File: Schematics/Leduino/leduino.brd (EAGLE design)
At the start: 88.6 x 63.5 mm, 31 parts, among them J1 POWER_JACKCOMBO

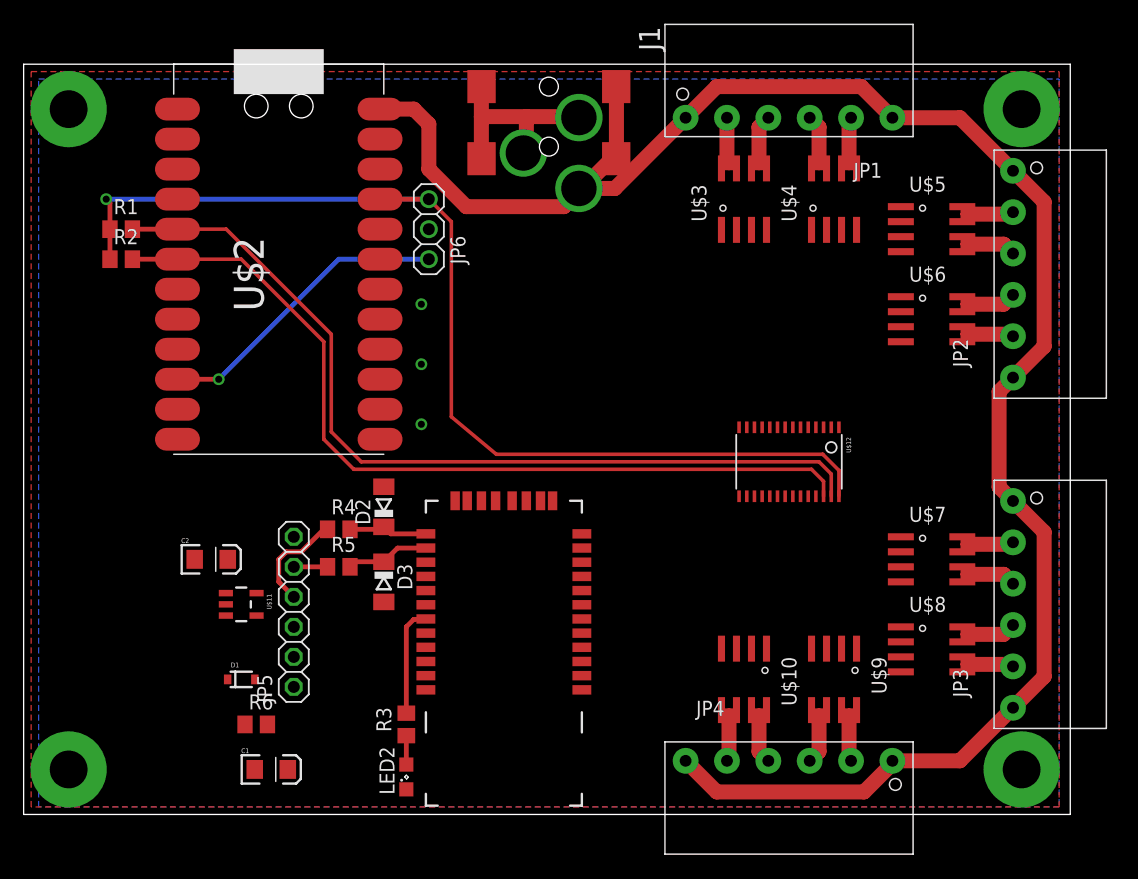
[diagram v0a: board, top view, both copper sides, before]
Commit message: Making progress, attempting to hack the autorouter
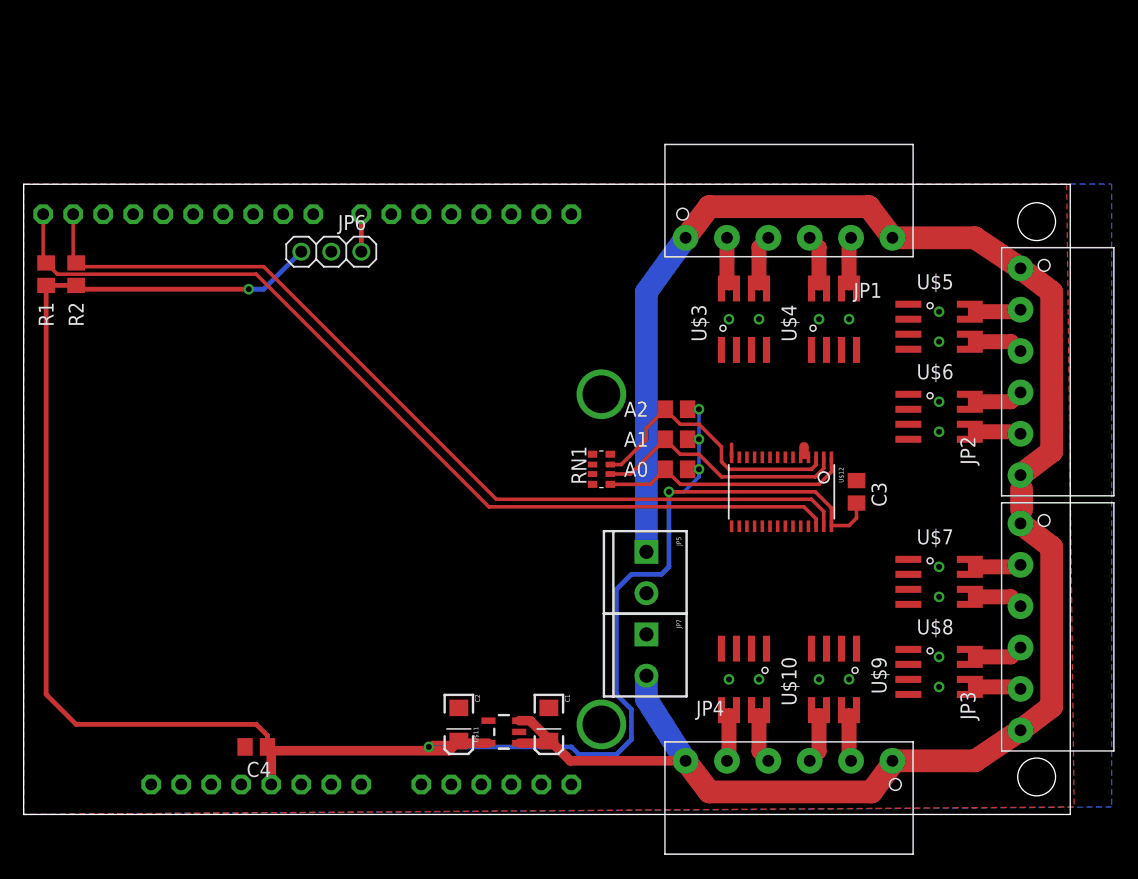
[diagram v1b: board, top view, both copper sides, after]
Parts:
- removed D1: (no value), SparkFun:SOD-323
- removed D2: 3.3V, diode:SOD80C
- removed D3: 3.3v, diode:SOD80C
- removed J1: POWER_JACKCOMBO, SparkFun-Connectors:POWER_JACK_COMBO
- removed LED2: RED, led:SML0805
- removed R3: 1K, rcl:R0805
- removed R4, R5: 10K, rcl:R0805
- removed R6: 0Ohm DNP, rcl:R0805
- removed U$2: PRO_MICRO, Leduino:ARDUINO_PRO_MICRO_SMD
- added A0, A1, A2: 0 Ohm DNP, rcl:R0805
- added C3, C4: .1uF, rcl:C0805
- added JP7: M023.5MM, SparkFun-Connectors:SCREWTERMINAL-3.5MM-2
- added RN1: (no value), resistor-dil:EXB38V
- JP5: value FTDI_CABLE -> M023.5MM; device Leduino:1X06 -> SparkFun-Connectors:SCREWTERMINAL-3.5MM-2
- U$1: value BLUETOOTH-RN41" -> SHIELD; device Leduino:RN41 -> Leduino:ARDUINOR3
- U$11: value MIC5219-3.3YM5 -> MIC5219-5.0YM5
- moved U$1 60.3 mm to (-17.1, 0.00), turned to 0 degrees
- moved JP5 30.3 mm to (52.7, 22.2), turned to 270 degrees
- moved C2 25.2 mm to (36.8, 7.62), turned to 270 degrees
- moved U$11 24.7 mm to (40.6, 6.99), turned to 90 degrees
- moved C1 23.8 mm to (44.5, 7.62), turned to 270 degrees
- moved JP1 10.2 mm to (64.8, 50.8)
- moved U$3 10.2 mm to (61.0, 41.9)
- moved U$4 10.2 mm to (68.6, 41.9)
- moved JP6 8.47 mm to (26.0, 47.6), turned to 0 degrees
- moved U$5 8.28 mm to (77.5, 41.3)
- moved JP2 8.28 mm to (86.4, 37.5)
- moved U$6 8.28 mm to (77.5, 33.7)
- moved R2 6.48 mm to (1.91, 45.7), turned to 90 degrees
- moved R1 5.39 mm to (4.45, 45.7), turned to 90 degrees
- moved U$12 2.62 mm to (64.1, 27.3)
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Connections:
- removed net CTS: JP5.2
- removed net FTDI_VCC: D1.2, JP5.3
- removed net N$13: R3.2, U$1.19
- removed net N$14: D2.C, R4.2, U$1.13
- removed net N$38: LED2.A, R3.1
- removed net RTS: JP5.6
- removed net RX: JP5.5, R5.1, U$2.2
- removed net TX: JP5.4, R4.1, U$2.1
- removed net V33: C2.A, R6.2, U$1.11, U$11.5
- new net N$16: A1.1, RN1.6, U$12.2
- new net N$21: A2.1, RN1.7, U$12.3
- net GND: now also C3.2, C4.2, JP5.2, JP7.1, RN1.1, RN1.2, RN1.3, RN1.4, U$1.GND, U$1.GND1, U$1.GND2; no longer D2.A, D3.A, J1.GND, J1.GND@1, JP5.1, LED2.C, U$1.1, U$1.12, U$1.28, U$1.29, U$12.1, U$12.2, U$12.3, U$2.19, U$2.20, U$2.23, U$2.3, U$2.4, U$2.8, U$2.9
- net IR_INT: now also U$1.D7; no longer U$2.10
- net N$15: now also A0.1, RN1.5, U$12.1; no longer D3.C, R5.2, U$1.14
- net SCL: now also U$1.SCL; no longer U$2.6
- net SDA: now also U$1.SDA; no longer U$2.5
- net VCC: now also A0.2, A1.2, A2.2, C2.A, C3.1, C4.1, U$1.5V, U$11.5; no longer R6.1, U$2.21
- net VIN: now also JP5.1, JP7.2; no longer D1.1, J1.POWER, U$2.24
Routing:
- net VCC: track 92.6 -> 180.6 mm, vias 1 -> 6
- net N$21: track 0.00 -> 23.6 mm
- net IR_INT: track 25.5 -> 3.17 mm, vias 1 -> 0
- net N$16: track 0.00 -> 21.8 mm
- net N$15: track 7.08 -> 21.4 mm
- net VIN: track 149.2 -> 162.0 mm
- net N$13: track 9.24 -> 0.00 mm
- net TX: track 8.88 -> 0.00 mm
- net N$14: track 6.75 -> 0.00 mm
- net SCL: track 73.1 -> 79.0 mm
- net SDA: track 74.4 -> 77.6 mm
- net GND: track 0.00 -> 2.87 mm, vias 7 -> 18
- net RX: track 2.86 -> 0.00 mm
- net N$38: track 2.45 -> 0.00 mm
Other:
- board size 88.6 x 63.5 mm -> 88.6 x 53.3 mm

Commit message: Finished Layout, cleared DRC
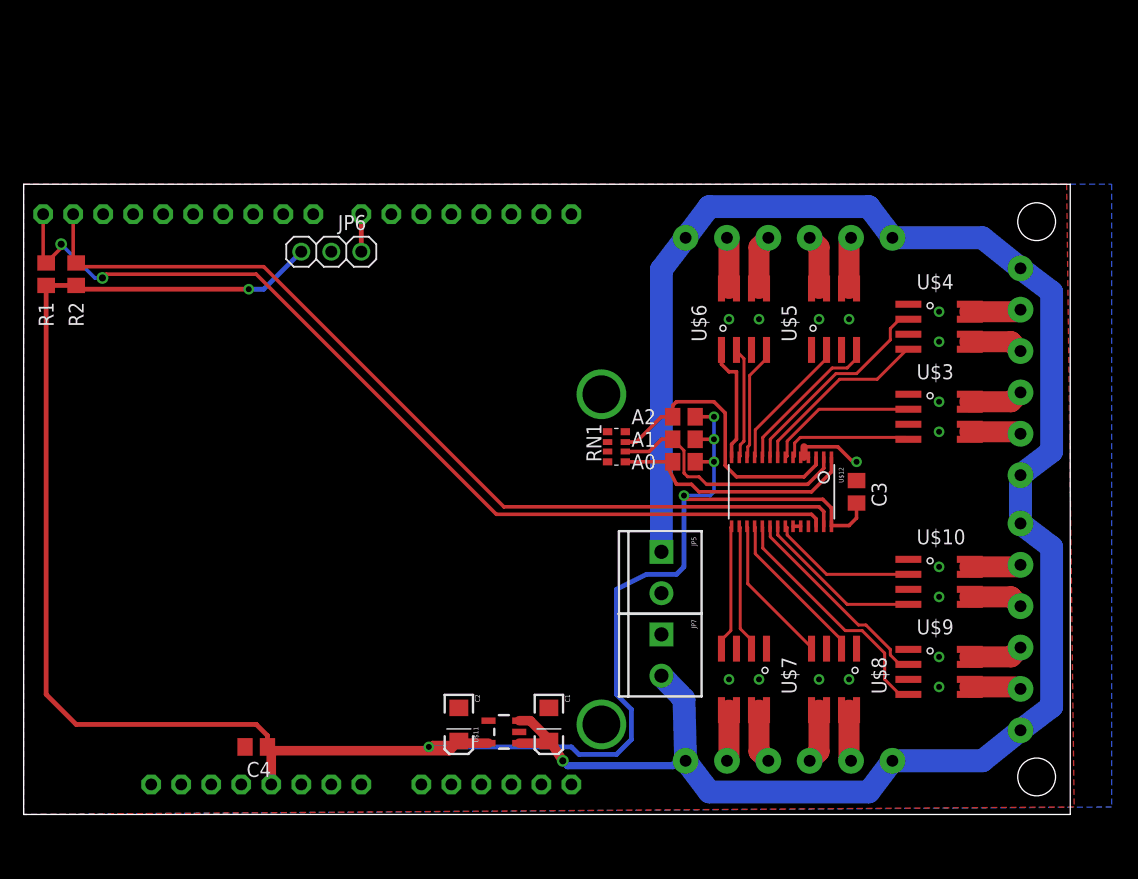
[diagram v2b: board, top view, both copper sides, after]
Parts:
- U$10, U$3, U$4, U$5, U$6, U$7, U$8, U$9: value (none) -> DMN6040SSD
- moved JP3 25.4 mm to (64.8, 2.54), flipped to the bottom, turned to 180 degrees
- moved JP4 25.4 mm to (86.4, 15.9), flipped to the bottom, turned to 90 degrees
- moved JP1 25.4 mm to (86.4, 37.5), flipped to the bottom, turned to 90 degrees
- moved JP2 25.4 mm to (64.8, 50.8), flipped to the bottom, turned to 0 degrees
- moved U$10 18.5 mm to (77.5, 19.7), turned to 270 degrees
- moved U$7 18.5 mm to (61.0, 11.4), turned to 180 degrees
- moved U$3 18.5 mm to (77.5, 33.7), turned to 270 degrees
- moved U$6 18.5 mm to (61.0, 41.9), turned to 0 degrees
- moved U$4 8.91 mm to (77.5, 41.3), turned to 270 degrees
- moved U$5 8.91 mm to (68.6, 41.9), turned to 0 degrees
- moved U$8 8.91 mm to (68.6, 11.4), turned to 180 degrees
- moved U$9 8.91 mm to (77.5, 12.1), turned to 270 degrees
- moved RN1 2.29 mm to (50.2, 31.1)
- moved JP5 1.27 mm to (54.0, 22.2)
- moved JP7 1.27 mm to (54.0, 15.2)
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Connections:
- net N$1: now also U$3.5, U$3.6; no longer U$3.7, U$3.8
- net N$10: now also U$5.7, U$5.8; no longer U$5.5, U$5.6
- net N$11: now also U$6.7, U$6.8; no longer U$6.5, U$6.6
- net N$12: now also U$6.5, U$6.6; no longer U$6.7, U$6.8
- net N$17: now also U$7.5, U$7.6; no longer U$7.7, U$7.8
- net N$18: now also U$7.7, U$7.8; no longer U$7.5, U$7.6
- net N$19: now also U$8.7, U$8.8; no longer U$8.5, U$8.6
- net N$2: now also U$3.7, U$3.8; no longer U$3.5, U$3.6
- net N$20: now also U$8.5, U$8.6; no longer U$8.7, U$8.8
- net N$3: now also U$4.7, U$4.8; no longer U$4.5, U$4.6
- net N$4: now also U$4.5, U$4.6; no longer U$4.7, U$4.8
- net N$5: now also U$9.5, U$9.6; no longer U$9.7, U$9.8
- net N$6: now also U$9.7, U$9.8; no longer U$9.5, U$9.6
- net N$7: now also U$10.7, U$10.8; no longer U$10.5, U$10.6
- net N$8: now also U$10.5, U$10.6; no longer U$10.7, U$10.8
- net N$9: now also U$5.5, U$5.6; no longer U$5.7, U$5.8
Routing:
- net PWM12: track 0.00 -> 20.6 mm
- net PWM3: track 0.00 -> 18.0 mm
- net PWM13: track 0.00 -> 17.3 mm
- net PWM2: track 0.00 -> 15.6 mm
- net GND: track 2.87 -> 17.9 mm, vias 18 -> 19
- net PWM14: track 0.00 -> 14.2 mm
- net PWM11: track 0.00 -> 13.4 mm
- net PWM4: track 0.00 -> 13.1 mm
- net PWM1: track 0.00 -> 12.8 mm
- net PWM10: track 0.00 -> 12.6 mm
- net PWM15: track 0.00 -> 12.5 mm
- net PWM5: track 0.00 -> 11.6 mm
- net PWM0: track 0.00 -> 11.2 mm
- net PWM9: track 0.00 -> 10.8 mm
- net PWM8: track 0.00 -> 10.7 mm
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
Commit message: Cleaned up silkscreen, passed freedDFM
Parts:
- JP1, JP2: value (none) -> M023.5MM; device Leduino:1X06-3.5M-RA -> SparkFun-Connectors:SCREWTERMINAL-3.5MM-2
- JP3: device Leduino:1X06-3.5M-RA -> adafruit:1X03
- JP5, JP7: value M023.5MM -> (none); device SparkFun-Connectors:SCREWTERMINAL-3.5MM-2 -> Leduino:1X06-3.5M-RA
- JP6: device adafruit:1X03 -> Leduino:1X06-3.5M-RA
- moved JP3 59.4 mm to (26.0, 47.6), flipped to the top, turned to 0 degrees
- moved JP6 59.4 mm to (64.8, 2.54), flipped to the bottom, turned to 180 degrees
- moved JP1 39.3 mm to (54.0, 15.2), flipped to the top, turned to 270 degrees
- moved JP7 32.4 mm to (86.4, 15.9), flipped to the bottom, turned to 90 degrees
- moved JP2 30.5 mm to (54.0, 22.2), flipped to the top, turned to 270 degrees
- moved JP5 30.5 mm to (64.8, 50.8), flipped to the bottom, turned to 0 degrees
- moved JP4 21.6 mm to (86.4, 37.5)
- renumbered U$1 to S1, U$10 to U10, U$11 to U1, U$12 to U2, U$3 to U3, U$4 to U4, U$5 to U5, U$6 to U6, U$7 to U7, U$8 to U8, U$9 to U9
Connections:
- net GND: now also JP1.1, JP2.2, JP3.2; no longer JP5.2, JP6.2, JP7.1
- net IR_INT: now also JP3.3; no longer JP6.3
- net N$1: now also JP4.2; no longer JP1.2
- net N$10: now also JP5.3; no longer JP2.3
- net N$11: now also JP5.5; no longer JP2.5
- net N$12: now also JP5.4; no longer JP2.4
- net N$17: now also JP6.2; no longer JP3.2
- net N$18: now also JP6.3; no longer JP3.3
- net N$19: now also JP6.5; no longer JP3.5
- net N$2: now also JP4.3; no longer JP1.3
- net N$20: now also JP6.4; no longer JP3.4
- net N$3: now also JP4.5; no longer JP1.5
- net N$4: now also JP4.4; no longer JP1.4
- net N$5: now also JP7.2; no longer JP4.2
- net N$6: now also JP7.3; no longer JP4.3
- net N$7: now also JP7.5; no longer JP4.5
- net N$8: now also JP7.4; no longer JP4.4
- net N$9: now also JP5.2; no longer JP2.2
- net VCC: now also JP3.1; no longer JP6.1
- net VIN: now also JP1.2, JP5.6, JP6.1, JP6.6, JP7.1, JP7.6; no longer JP1.1, JP1.6, JP2.6, JP3.1, JP3.6, JP7.2
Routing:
- net GND: vias 19 -> 23
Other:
- board text added: "0"
- board text added: "1"
- board text added: "10"
- board text added: "11"
- board text added: "12"
- board text added: "13"
- board text added: "14"
- board text added: "15"
- board text added: "2"
- board text added: "3"
- board text added: "4"
- board text added: "5"
- board text added: "6"
- board text added: "7"
- board text added: "8"
- board text added: "9"
- board text added: "LEDuino PWM Sheild Version 0.1.0 (C) 2014, Nathaniel Chapman nathanielchapman.com"

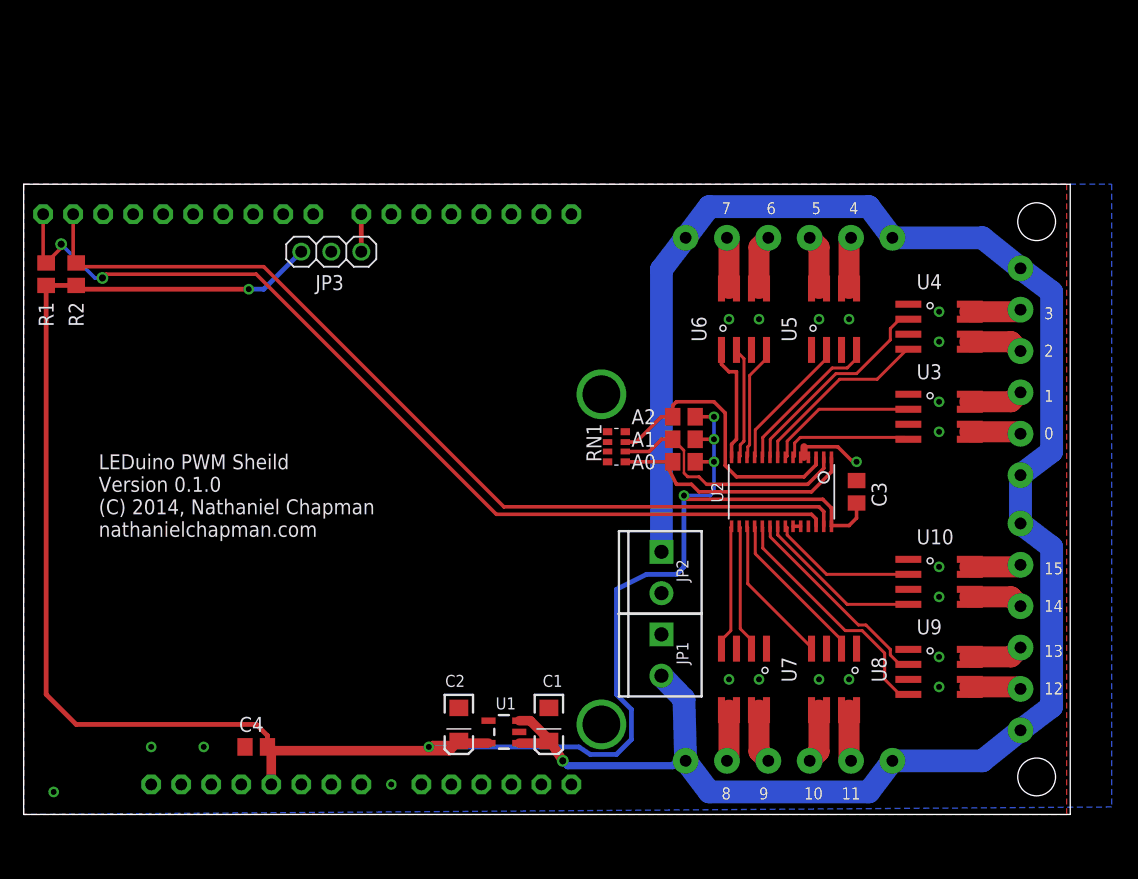
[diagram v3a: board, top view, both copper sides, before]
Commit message: Designed and Laid out Board Rev 2.0 ready for review
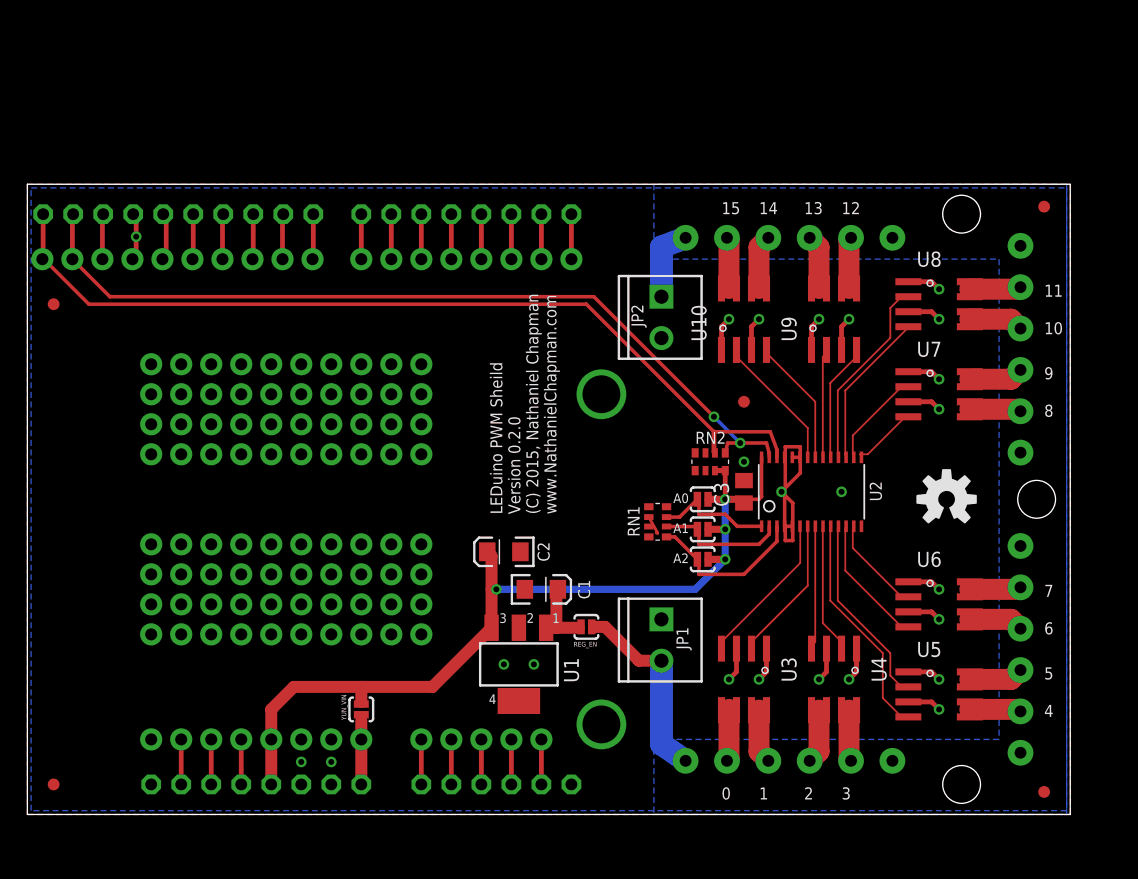
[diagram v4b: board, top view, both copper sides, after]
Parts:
- removed C4: .1uF, rcl:C0805
- removed R1, R2: 10K, rcl:R0805
- added JP10: (no value), SparkFun-Connectors:1X05_NO_SILK
- added JP8, JP9: (no value), SparkFun-Connectors:1X08_NO_SILK
- added NC1, NC2, NC3, NC4: PROTOBOARD5X4, Leduino:5X4_PROTO
- added REG_EN, YUN_VIN: (no value), Leduino:SJ_2S-NO
- added RN2: 10K, resistor-dil:EXB38V
- added U$1, U$2, U$4, U$5: (no value), Pro_Micro:FIDUCIAL-1X2
- added U$3: (no value), Pro_Micro:OSHW-LOGO-M
- A0, A1, A2: value 0 Ohm DNP -> (none); device rcl:R0805 -> Leduino:SJ_2S-NO
- JP3: device adafruit:1X03 -> SparkFun-Connectors:1X10_NO_SILK
- RN1: value (none) -> 10K
- U1: value MIC5219-5.0YM5 -> MIC39100-5.0WS; device SparkFun:SOT23-5 -> Leduino:SOT223
- moved JP5 42.7 mm to (86.4, 14.0), turned to 90 degrees
- moved JP6 42.7 mm to (86.4, 39.4), turned to 90 degrees
- moved JP4 41.1 mm to (64.8, 2.54), turned to 180 degrees
- moved JP7 41.1 mm to (64.8, 50.8), turned to 0 degrees
- moved U8 33.0 mm to (77.5, 43.2), turned to 270 degrees
- moved U5 33.0 mm to (77.5, 10.2), turned to 270 degrees
- moved U4 31.1 mm to (68.6, 11.4), turned to 180 degrees
- moved U9 31.1 mm to (68.6, 41.9), turned to 0 degrees
- moved U7 29.2 mm to (77.5, 35.6), turned to 270 degrees
- moved U6 29.2 mm to (77.5, 17.8), turned to 270 degrees
- moved U3 27.7 mm to (61.0, 11.4), turned to 180 degrees
- moved U10 27.7 mm to (61.0, 41.9), turned to 0 degrees
- moved JP3 24.5 mm to (1.59, 47.0)
- moved JP2 21.6 mm to (54.0, 43.8)
- moved C2 15.1 mm to (40.6, 22.2), turned to 180 degrees
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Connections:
- removed net IR_INT: JP3.3, S1.D7
- new net 3.3V: JP9.4, S1.3V
- new net A0: JP10.5, S1.A0
- new net A1: JP10.4, S1.A1
- new net A2: JP10.3, S1.A2
- new net A3: JP10.2, S1.A3
- new net A4: JP10.1, S1.A4
- new net A5: S1.A5
- new net AREF: JP3.3, S1.AREF
- new net D0: JP8.8, S1.D0
- new net D1: JP8.7, S1.D1
- new net D10: JP3.8, S1.D10
- new net D11: JP3.7, S1.D11
- new net D12: JP3.6, S1.D12
- new net D13: JP3.5, S1.D13
- new net D2: JP8.6, S1.D2
- new net D3: JP8.5, S1.D3
- new net D4: JP8.4, S1.D4
- new net D5: JP8.3, S1.D5
- new net D6: JP8.2, S1.D6
- new net D7: JP8.1, S1.D7
- new net D8: JP3.10, S1.D8
- new net D9: JP3.9, S1.D9
- new net IOREF: JP9.2, S1.IOREF
- new net N$13: C1.A, REG_EN.2, U1.1
- new net NC: JP9.1
- new net RES: JP9.3, S1.RESET
- new net VIN_A: JP9.8, S1.VIN, YUN_VIN.1
- net GND: now also JP3.4, JP9.6, JP9.7, RN1.8, U1.4; no longer C4.2, JP3.2
- net N$15: now also RN1.7; no longer RN1.5
- net N$21: now also RN1.5; no longer RN1.7
- net SCL: now also JP3.1, RN2.2; no longer R2.2
- net SDA: now also JP3.2, RN2.1; no longer R1.2
- net VCC: now also JP9.5, RN2.7, RN2.8, U1.3, YUN_VIN.2; no longer C4.1, JP3.1, R1.1, R2.1, U1.5
- net VIN: now also REG_EN.1; no longer C1.A, U1.1, U1.3
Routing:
- net VIN: track 162.1 -> 23.0 mm, vias 1 -> 0
- net VCC: track 181.4 -> 77.3 mm, vias 6 -> 4
- net GND: track 17.9 -> 72.1 mm, vias 23 -> 26
- net N$15: track 21.5 -> 10.3 mm
- net N$21: track 24.4 -> 13.8 mm
- net PWM12: track 20.6 -> 10.0 mm
- net N$16: track 21.4 -> 11.0 mm
- net PWM13: track 17.3 -> 9.22 mm
- net PWM3: track 18.0 -> 11.0 mm
- net N$13: track 0.00 -> 6.33 mm
- net PWM4: track 13.1 -> 19.2 mm
- net VIN_A: track 0.00 -> 5.90 mm
- net SDA: track 77.6 -> 72.2 mm, vias 0 -> 2
- net SCL: track 80.8 -> 75.5 mm, vias 2 -> 0
- net PWM2: track 15.6 -> 10.5 mm
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- added copper zone on layer 16, net VIN
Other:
- board size 88.6 x 53.3 mm -> 88.3 x 53.3 mm
- board text added: "+"
- board text added: "-"
- board text added: "LEDuino PWM Sheild Version 0.2.0 (C) 2015, Nathaniel Chapman www.NathanielChapman.com"
- board text removed: "LEDuino PWM Sheild Version 0.1.0 (C) 2014, Nathaniel Chapman nathanielchapman.com"
